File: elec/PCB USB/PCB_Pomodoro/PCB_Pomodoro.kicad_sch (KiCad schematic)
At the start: 0 parts

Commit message: debut du projet avec dimensions dans le PCB
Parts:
- added J1: USB_C_Receptacle_USB2.0_14P, symbol Connector:USB_C_Receptacle_USB2.0_14P
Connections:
- new net GND: J1.A1 (GND), J1.A12 (GND), J1.B1 (GND), J1.B12 (GND), J1.S1 (SHIELD)
- new net VCC: J1.A4 (VBUS), J1.A9 (VBUS), J1.B4 (VBUS), J1.B9 (VBUS)

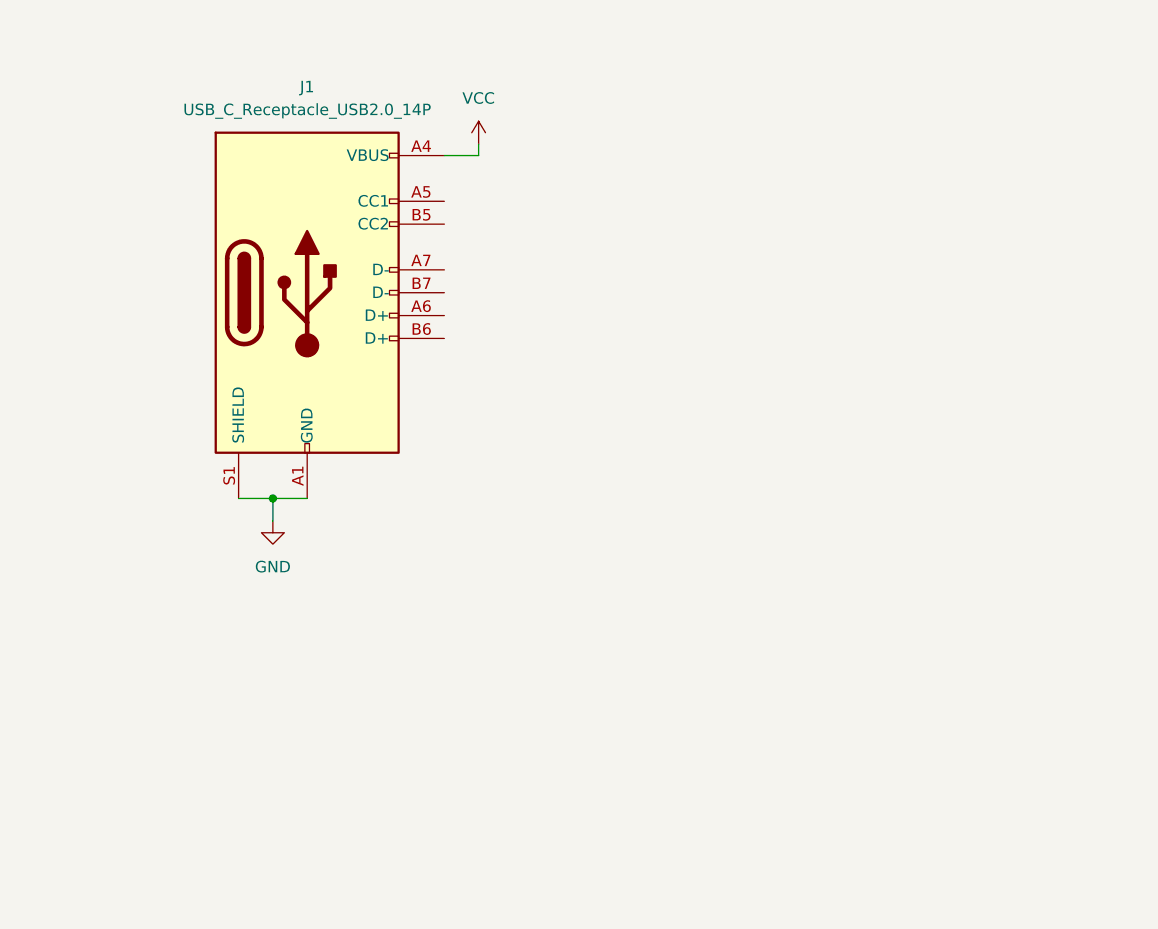
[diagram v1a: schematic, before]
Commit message: Ajout des USB A et C
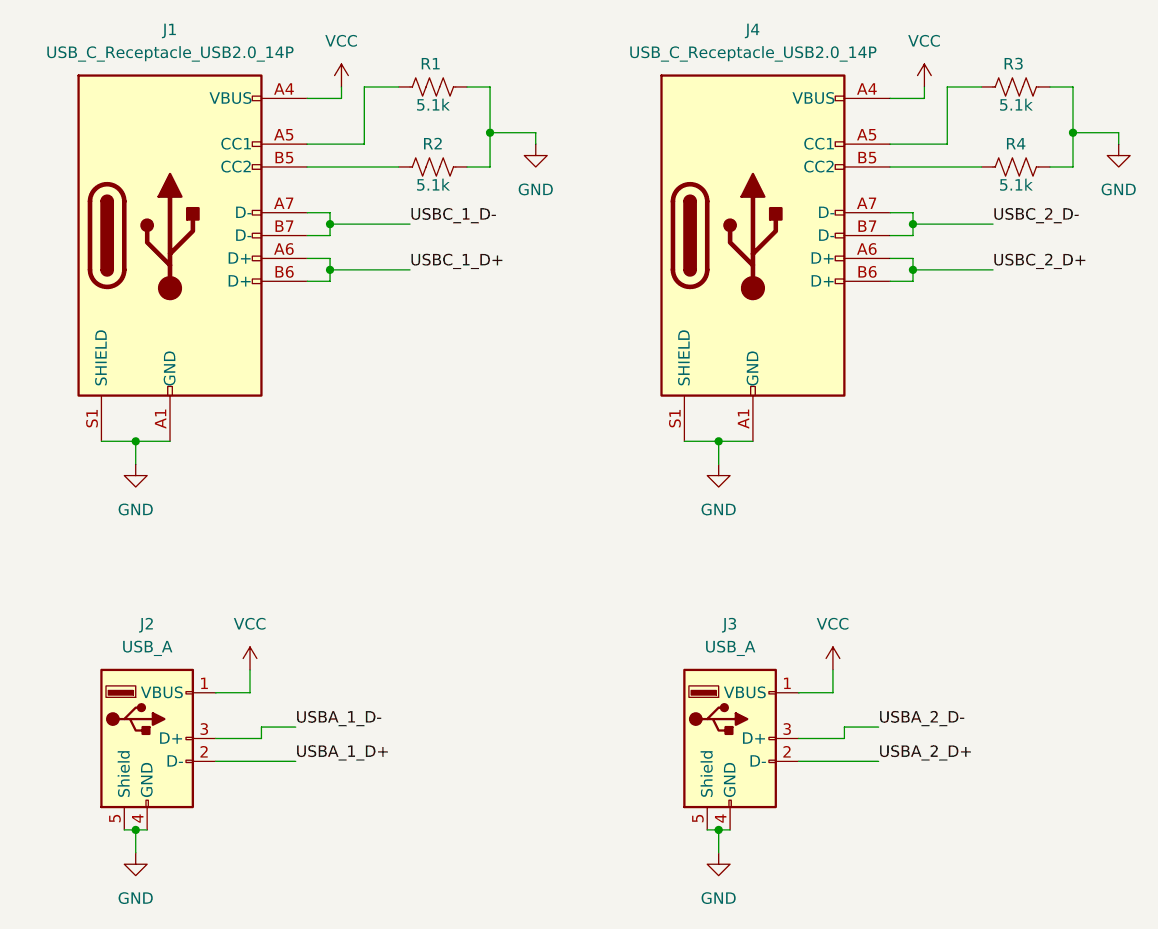
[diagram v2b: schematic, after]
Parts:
- added J2, J3: USB_A, symbol Connector:USB_A
- added J4: USB_C_Receptacle_USB2.0_14P, symbol Connector:USB_C_Receptacle_USB2.0_14P
- added R1, R2, R3, R4: 5.1k, symbol Device:R_US
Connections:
- net GND: now also J2.4 (GND), J2.5 (Shield), J3.4 (GND), J3.5 (Shield), J4.A1 (GND), J4.A12 (GND), J4.B1 (GND), J4.B12 (GND), J4.S1 (SHIELD), R1.2, R2.2, R3.2, R4.2
- net VCC: now also J2.1 (VBUS), J3.1 (VBUS), J4.A4 (VBUS), J4.A9 (VBUS), J4.B4 (VBUS), J4.B9 (VBUS)
- net at J1.A5 (CC1): now also R1.1
- net USBC_1_D+: now reaches J1.A6 (D+)
- net USBC_1_D+: now also J1.B6 (D+)
- net USBC_1_D-: now reaches J1.A7 (D-)
- net USBC_1_D-: now also J1.B7 (D-)
- net at J1.B5 (CC2): now also R2.1
- new net: J4.A5 (CC1), R3.1
- new net: J4.B5 (CC2), R4.1
- new net USBA_1_D+: J2.2 (D-)
- new net USBA_1_D-: J2.3 (D+)
- new net USBA_2_D+: J3.2 (D-)
- new net USBA_2_D-: J3.3 (D+)
- new net USBC_2_D+: J4.A6 (D+), J4.B6 (D+)
- new net USBC_2_D-: J4.A7 (D-), J4.B7 (D-)
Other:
- moved on the sheet: J1
